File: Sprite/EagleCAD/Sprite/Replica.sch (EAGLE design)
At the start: 25 parts, among them U1 CC430F5137, X1 26 MHz

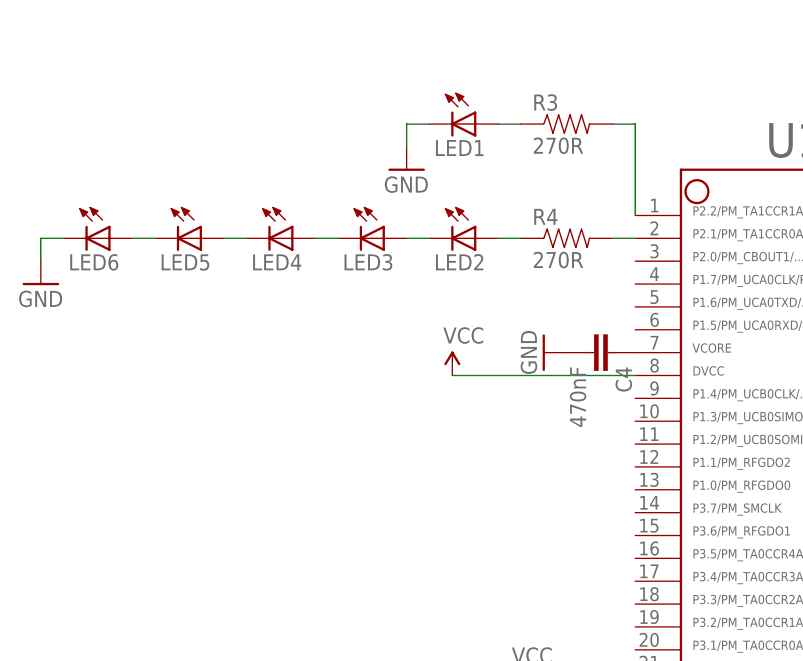
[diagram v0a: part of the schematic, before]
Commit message: Replica board - put each LED on it's own pin
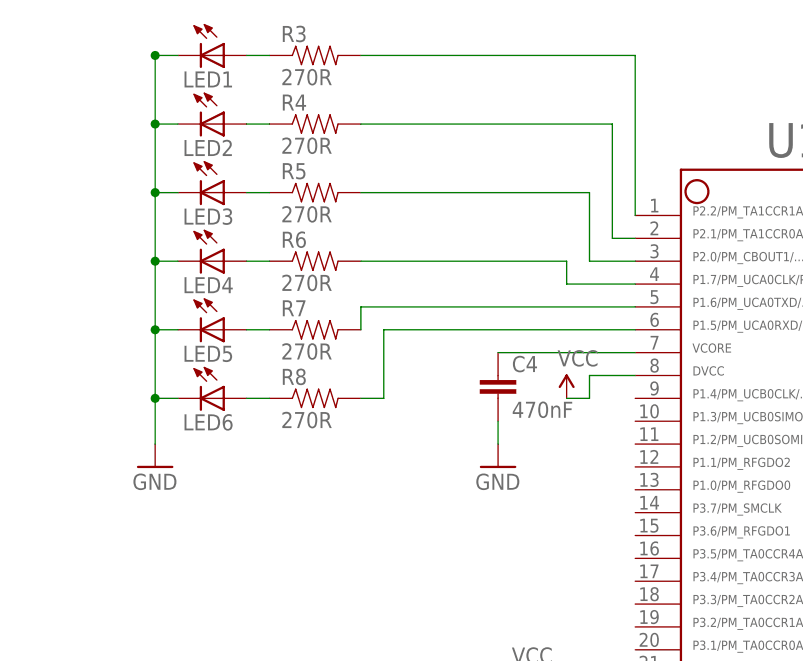
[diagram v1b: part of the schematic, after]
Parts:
- added R5, R6, R7, R8: 270R, SparkFun:RESISTOR0603-RES
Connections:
- net N$4 renamed VCORE
- new net N$13: R5.2, U1.3
- new net N$14: R6.2, U1.4
- new net N$15: R7.2, U1.5
- new net N$16: R8.2, U1.6
- net GND: now also LED2.C, LED3.C, LED4.C, LED5.C
- net N$10: now also R8.1; no longer LED5.C
- net N$7: now also R5.1; no longer LED2.C
- net N$8: now also R6.1; no longer LED3.C
- net N$9: now also R7.1; no longer LED4.C
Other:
- moved on the sheet: C4, LED1, LED2, LED3, LED4, LED5, LED6, R3, R4
